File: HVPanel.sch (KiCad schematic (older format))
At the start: 13 parts, among them U1 VICOR

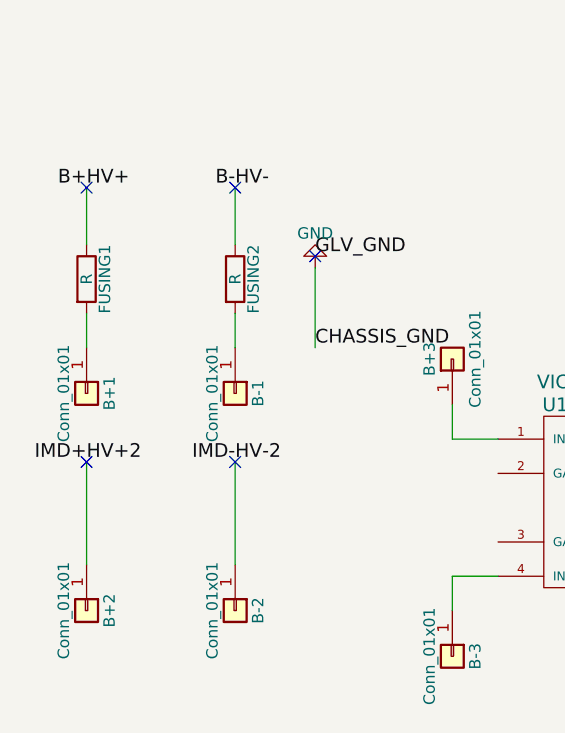
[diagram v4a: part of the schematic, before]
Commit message: deleted resistors, finished footprint
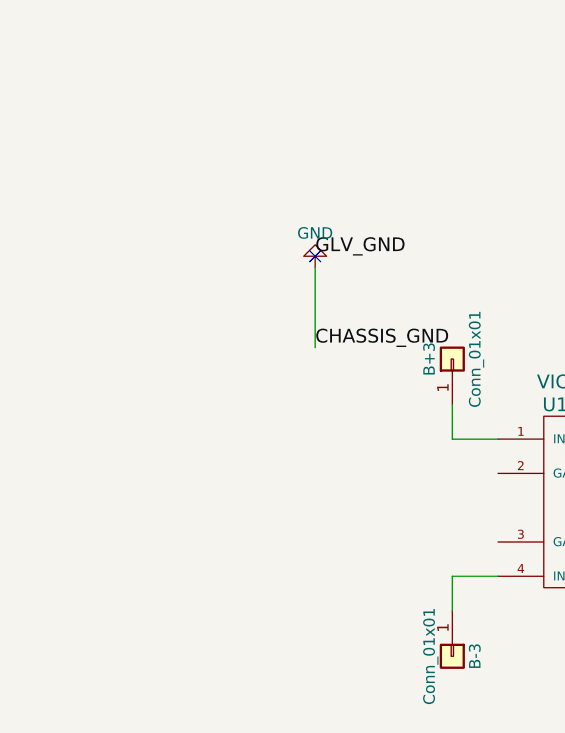
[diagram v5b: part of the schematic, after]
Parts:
- removed B+1, B+2, B-1, B-2: Conn_01x01, Wire_Pads:SolderWirePad_single_1-5mmDrill, symbol Conn_01x01
- removed FUSING1, FUSING2: R, TO_SOT_Packages_THT:TO-247-2_Vertical, symbol R
- JP1: footprint (none) -> Pin_Headers:Pin_Header_Straight_1x03_Pitch2.54mm
- JP2: footprint (none) -> Pin_Headers:Pin_Header_Straight_1x08_Pitch2.54mm
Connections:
- no-connect marks 5 -> 1
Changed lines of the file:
@@
 F 0 "JP1" H 5200 5000 50  0000 C CNN
 F 1 "Conn_01x03" H 5200 4600 50  0000 C CNN
-F 2 "" H 5200 4800 50  0001 C CNN
+F 2 "Pin_Headers:Pin_Header_Straight_1x03_Pitch2.54mm" H 5200 4800 50  0001 C CNN
 F 3 "" H 5200 4800 50  0001 C CNN
 	1    5200 4800
@@
 Text Label 2850 3450 0    60   ~ 0
 CHASSIS_GND
-Wire Wire Line
-	2500 3000 2500 2750
-Wire Wire Line
-	2500 3300 2500 3450
-$Comp
-L Conn_01x01 B-1
-U 1 1 5A2EC6F3
-P 2500 3650
-F 0 "B-1" H 2500 3750 50  0000 C CNN
-F 1 "Conn_01x01" H 2500 3550 50  0000 C CNN
-F 2 "Wire_Pads:SolderWirePad_single_1-5mmDrill" H 2500 3650 50  0001 C CNN
-F 3 "" H 2500 3650 50  0001 C CNN
-	1    2500 3650
-	0    1    1    0
-$EndComp
-$Comp
-L Conn_01x01 B+1
-U 1 1 5A2EC75B
-P 1850 3650
-F 0 "B+1" H 1850 3750 50  0000 C CNN
-F 1 "Conn_01x01" H 1850 3550 50  0000 C CNN
-F 2 "Wire_Pads:SolderWirePad_single_1-5mmDrill" H 1850 3650 50  0001 C CNN
-F 3 "" H 1850 3650 50  0001 C CNN
-	1    1850 3650
-	0    1    1    0
-$EndComp
-Text Label 2500 2750 2    60   ~ 0
-B-
-Text Label 2500 2750 0    60   ~ 0
-HV-
-Text Label 1850 2750 2    60   ~ 0
-B+
-Text Label 1850 2750 0    60   ~ 0
-HV+
-Wire Wire Line
-	2500 3950 2500 4400
-NoConn ~ 2500 3950
-NoConn ~ 2500 2750
 NoConn ~ 2850 3050
-$Comp
-L Conn_01x01 B-2
-U 1 1 5A2ECB68
-P 2500 4600
-F 0 "B-2" H 2500 4700 50  0000 C CNN
-F 1 "Conn_01x01" H 2500 4500 50  0000 C CNN
-F 2 "Wire_Pads:SolderWirePad_single_1-5mmDrill" H 2500 4600 50  0001 C CNN
-F 3 "" H 2500 4600 50  0001 C CNN
-	1    2500 4600
-	0    1    1    0
-$EndComp
-$Comp
-L Conn_01x01 B+2
-U 1 1 5A2ECBA0
-P 1850 4600
-F 0 "B+2" H 1850 4700 50  0000 C CNN
-F 1 "Conn_01x01" H 1850 4500 50  0000 C CNN
-F 2 "Wire_Pads:SolderWirePad_single_1-5mmDrill" H 1850 4600 50  0001 C CNN
-F 3 "" H 1850 4600 50  0001 C CNN
-	1    1850 4600
-	0    1    1    0
-$EndComp
-Text Label 2500 3950 0    60   ~ 0
-HV-2
-Text Label 2500 3950 2    60   ~ 0
-IMD-
-Text Label 1850 3950 0    60   ~ 0
-HV+2
-Text Label 1850 3950 2    60   ~ 0
-IMD+
 $Comp
 L Conn_01x14 U$3
@@
 F 0 "JP2" H 4900 2200 50  0000 C CNN
 F 1 "Conn_01x08" H 4900 1300 50  0000 C CNN
-F 2 "" H 4900 1800 50  0001 C CNN
+F 2 "Pin_Headers:Pin_Header_Straight_1x08_Pitch2.54mm" H 4900 1800 50  0001 C CNN
 F 3 "" H 4900 1800 50  0001 C CNN
 	1    4900 1800
@@
 Text Label 4500 2000 2    60   ~ 0
 D_OUT_LOW
-Wire Wire Line
-	1850 3450 1850 3300
-Wire Wire Line
-	1850 3000 1850 2750
-NoConn ~ 1850 2750
-Wire Wire Line
-	1850 4400 1850 3950
-NoConn ~ 1850 3950
 Text Notes 4800 2400 0    60   ~ 0
 To_IMD
-$Comp
-L R FUSING1
-U 1 1 5A664BC1
-P 1850 3150
-F 0 "FUSING1" V 1930 3150 50  0000 C CNN
-F 1 "R" V 1850 3150 50  0000 C CNN
-F 2 "TO_SOT_Packages_THT:TO-247-2_Vertical" V 1780 3150 50  0001 C CNN
-F 3 "" H 1850 3150 50  0001 C CNN
-	1    1850 3150
-	1    0    0    -1
-$EndComp
-$Comp
-L R FUSING2
-U 1 1 5A664C34
-P 2500 3150
-F 0 "FUSING2" V 2580 3150 50  0000 C CNN
-F 1 "R" V 2500 3150 50  0000 C CNN
-F 2 "TO_SOT_Packages_THT:TO-247-2_Vertical" V 2430 3150 50  0001 C CNN
-F 3 "" H 2500 3150 50  0001 C CNN
-	1    2500 3150
-	1    0    0    -1
-$EndComp
 $EndSCHEMATC
